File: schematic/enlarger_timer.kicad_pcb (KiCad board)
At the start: 2 copper layers, 85 x 85 mm, 60 parts, among them IC1 LD3985, J1 Screen, J2 LED, J3 5V, J4 ST-Link, J5 Start, J6 Switch_Light, SW1 Reset, SW2 But_Mem_Write, SW3 But_Mem_Read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

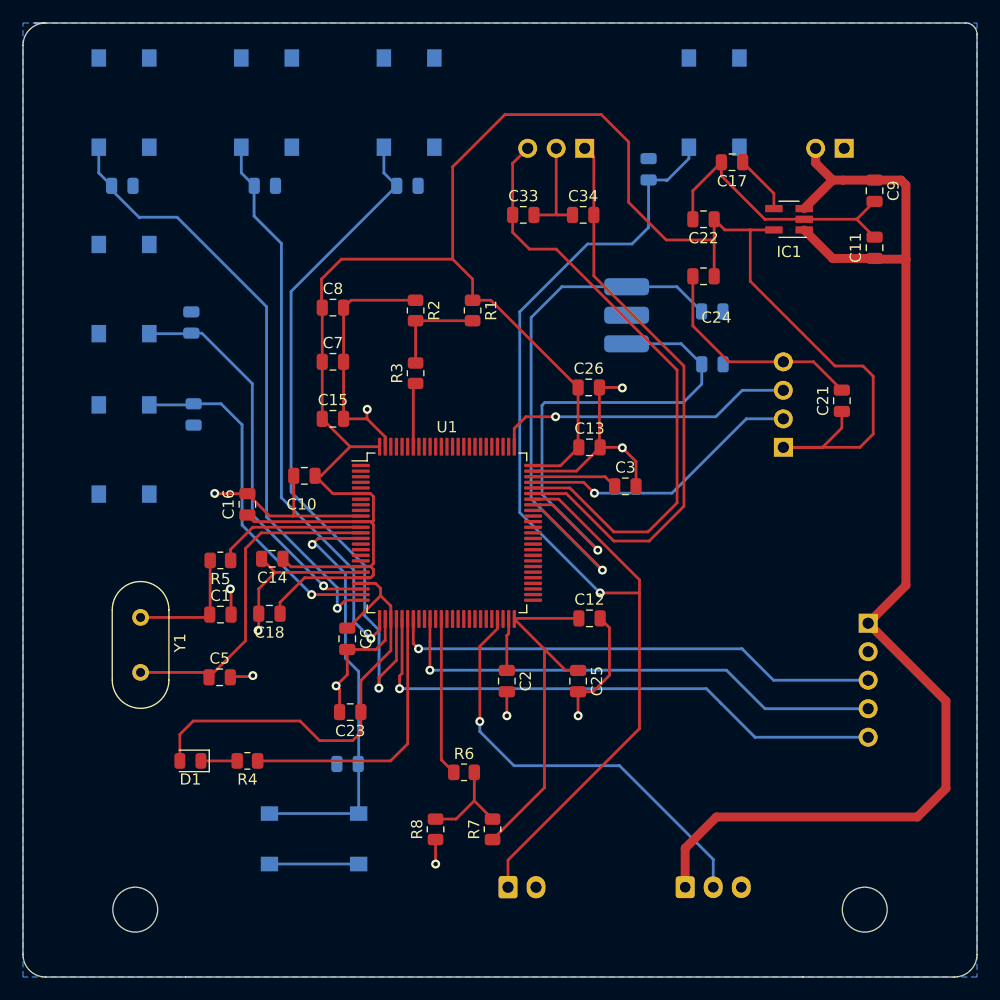
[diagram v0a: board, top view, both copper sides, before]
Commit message: Updated board: change button positions, add conneting holes
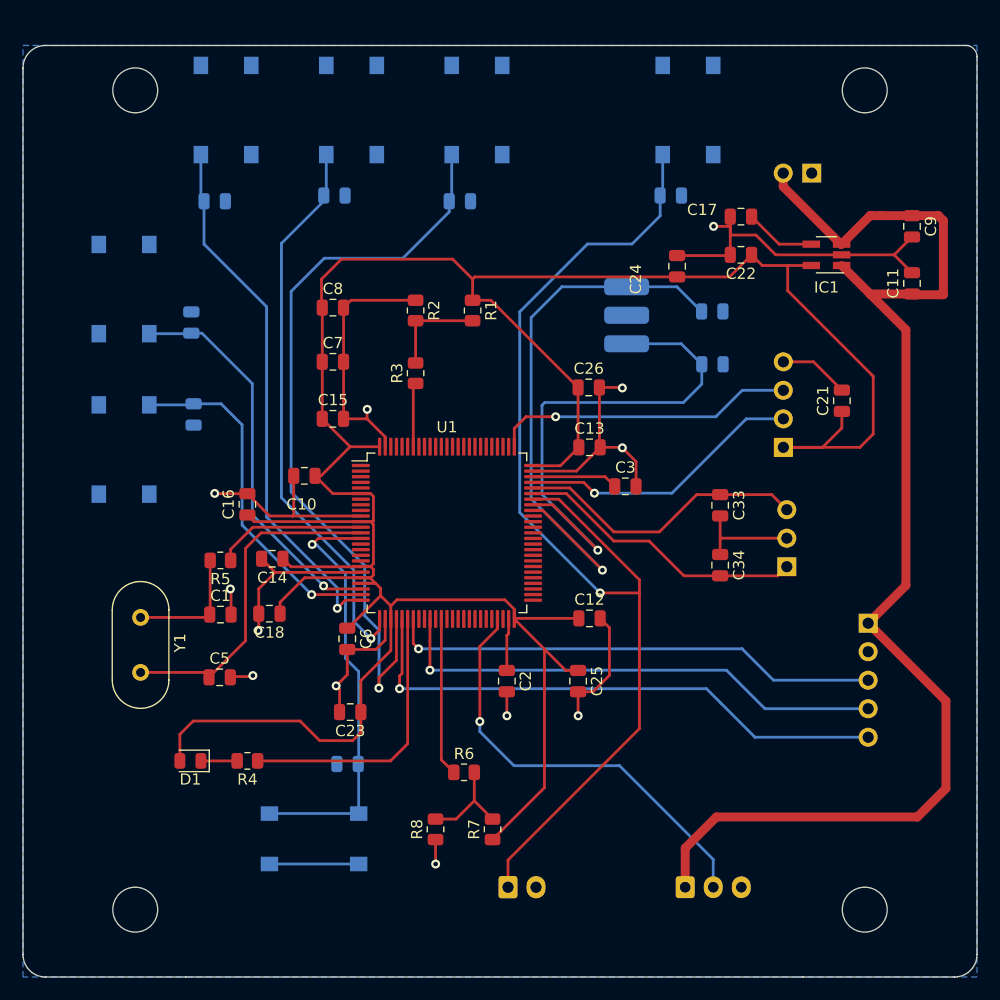
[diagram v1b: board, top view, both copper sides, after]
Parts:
- moved J6 41.4 mm to (183.1, 88.4), turned to 0 degrees
- moved C34 33.5 mm to (177.1, 88.3), turned to -90 degrees
- moved C33 31.3 mm to (177.1, 83.0), turned to -90 degrees
- moved SW5 9.12 mm to (133.1, 47.8)
- moved C30 8.34 mm to (132.1, 55.9)
- moved SW6 7.60 mm to (144.3, 47.8)
- moved C31 6.26 mm to (142.7, 55.4)
- moved SW7 6.08 mm to (155.4, 47.8)
- moved C17 4.91 mm to (179.0, 57.3)
- moved C32 4.87 mm to (153.9, 55.9)
- moved C11 4.60 mm to (194.2, 63.2)
- moved C9 4.60 mm to (194.2, 58.1)
- moved IC1 4.60 mm to (186.6, 60.7)
- moved C22 4.60 mm to (179.0, 60.7)
- moved J3 3.64 mm to (185.3, 53.4)
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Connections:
- U1 pad 25: /But_BRI -> /But_TIM
- U1 pad 29: /But_TIM -> /But_BRI
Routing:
- net /Switch_Daylight: track 55.1 -> 26.2 mm
- net /Switch_SafeLight: track 52.0 -> 26.0 mm
- net +3V3: track 271.2 -> 257.8 mm
- net GND: track 169.9 -> 160.4 mm, vias 11 -> 12
- net /But_TIM: track 54.3 -> 47.9 mm
- net /But_BRI: track 62.6 -> 67.6 mm
- net +5V: track 110.9 -> 114.1 mm
- net /But_Start: track 100.5 -> 97.8 mm
- net Net-(C17-Pad1): track 5.28 -> 6.34 mm
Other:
- board size 85 x 85 mm -> 85 x 83 mm
- board text added: "+3V3"
- board text added: "+5V"
- board text added: "Brightnes"
- board text added: "CLK"
- board text added: "CS"
- board text added: "Contrast"
- board text added: "DIN"
- board text added: "Data"
- board text added: "Day"
- board text added: "GND"
- board text added: "MR"
- board text added: "MW"
- board text added: "SWCLK"
- board text added: "SWDIO"
- board text added: "Safe"
- board text added: "Time"

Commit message: Added legend in silk
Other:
- board text added: "Start"
- board text added: "Ver 1.0"
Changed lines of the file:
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@@
+    (effects (font (size 1 1) (thickness 0.15)) (justify mirror))
+  )
+  (gr_text "Ver 1.0" (at 122.5804 51.9176) (layer "B.SilkS")
     (effects (font (size 1 1) (thickness 0.15)) (justify mirror))
   )
@@
     (effects (font (size 1 1) (thickness 0.15)) (justify mirror))
   )
+  (gr_text "Start" (at 178.4096 47.6504 90) (layer "B.SilkS")
+    (effects (font (size 1 1) (thickness 0.15)) (justify mirror))
+  )

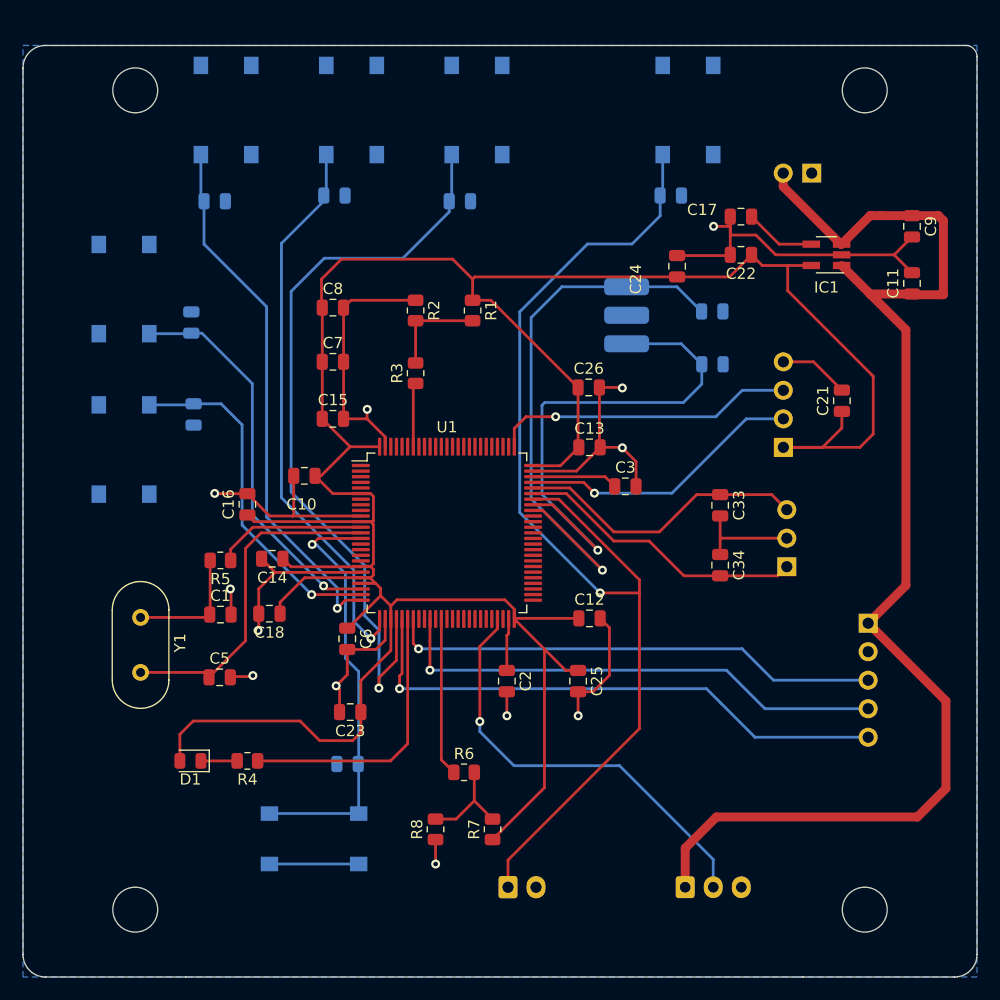
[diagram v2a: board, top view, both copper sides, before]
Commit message: Updated schematic: fixed board dimentions
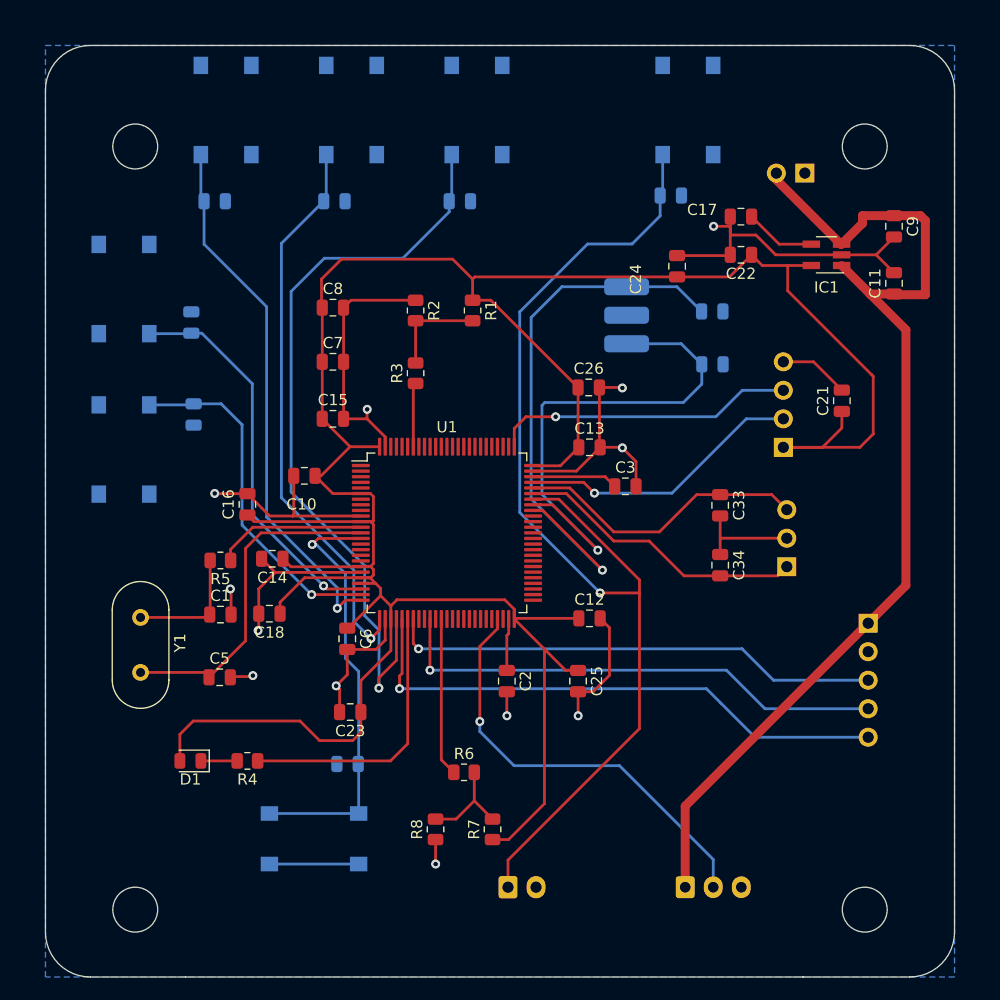
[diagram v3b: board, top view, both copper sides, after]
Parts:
- moved C11 1.60 mm to (192.6, 63.2)
- moved C9 1.60 mm to (192.6, 58.1)
- moved J3 0.61 mm to (184.7, 53.4)
- moved C31 0.51 mm to (142.7, 55.9)
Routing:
- net +5V: track 114.1 -> 95.3 mm
- net GND: track 160.4 -> 158.8 mm
- net +3V3: track 257.8 -> 258.6 mm
- net /But_CON: track 50.1 -> 50.6 mm
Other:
- board size 85 x 83 mm -> 81 x 83 mm
